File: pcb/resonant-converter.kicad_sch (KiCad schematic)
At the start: 103 parts, among them J1 Banana_Jack_Keystone_575-8, J2 Banana_Jack_Keystone_575-8, J3 Banana_Jack_Keystone_575-8, J4 Banana_Jack_Keystone_575-8, J6 Molex_KK_1x4_0470531000, Q1 MDU04N010VRH, Q2 MDU04N010VRH, Q3 HSU30N20, Q4 HSU30N20, T1 B66206W1110T001, U1 UCC256610DDBR, U2 TEA2096T/1J, U4 PC817X2CSP9F, U5 TL431AIDBVR

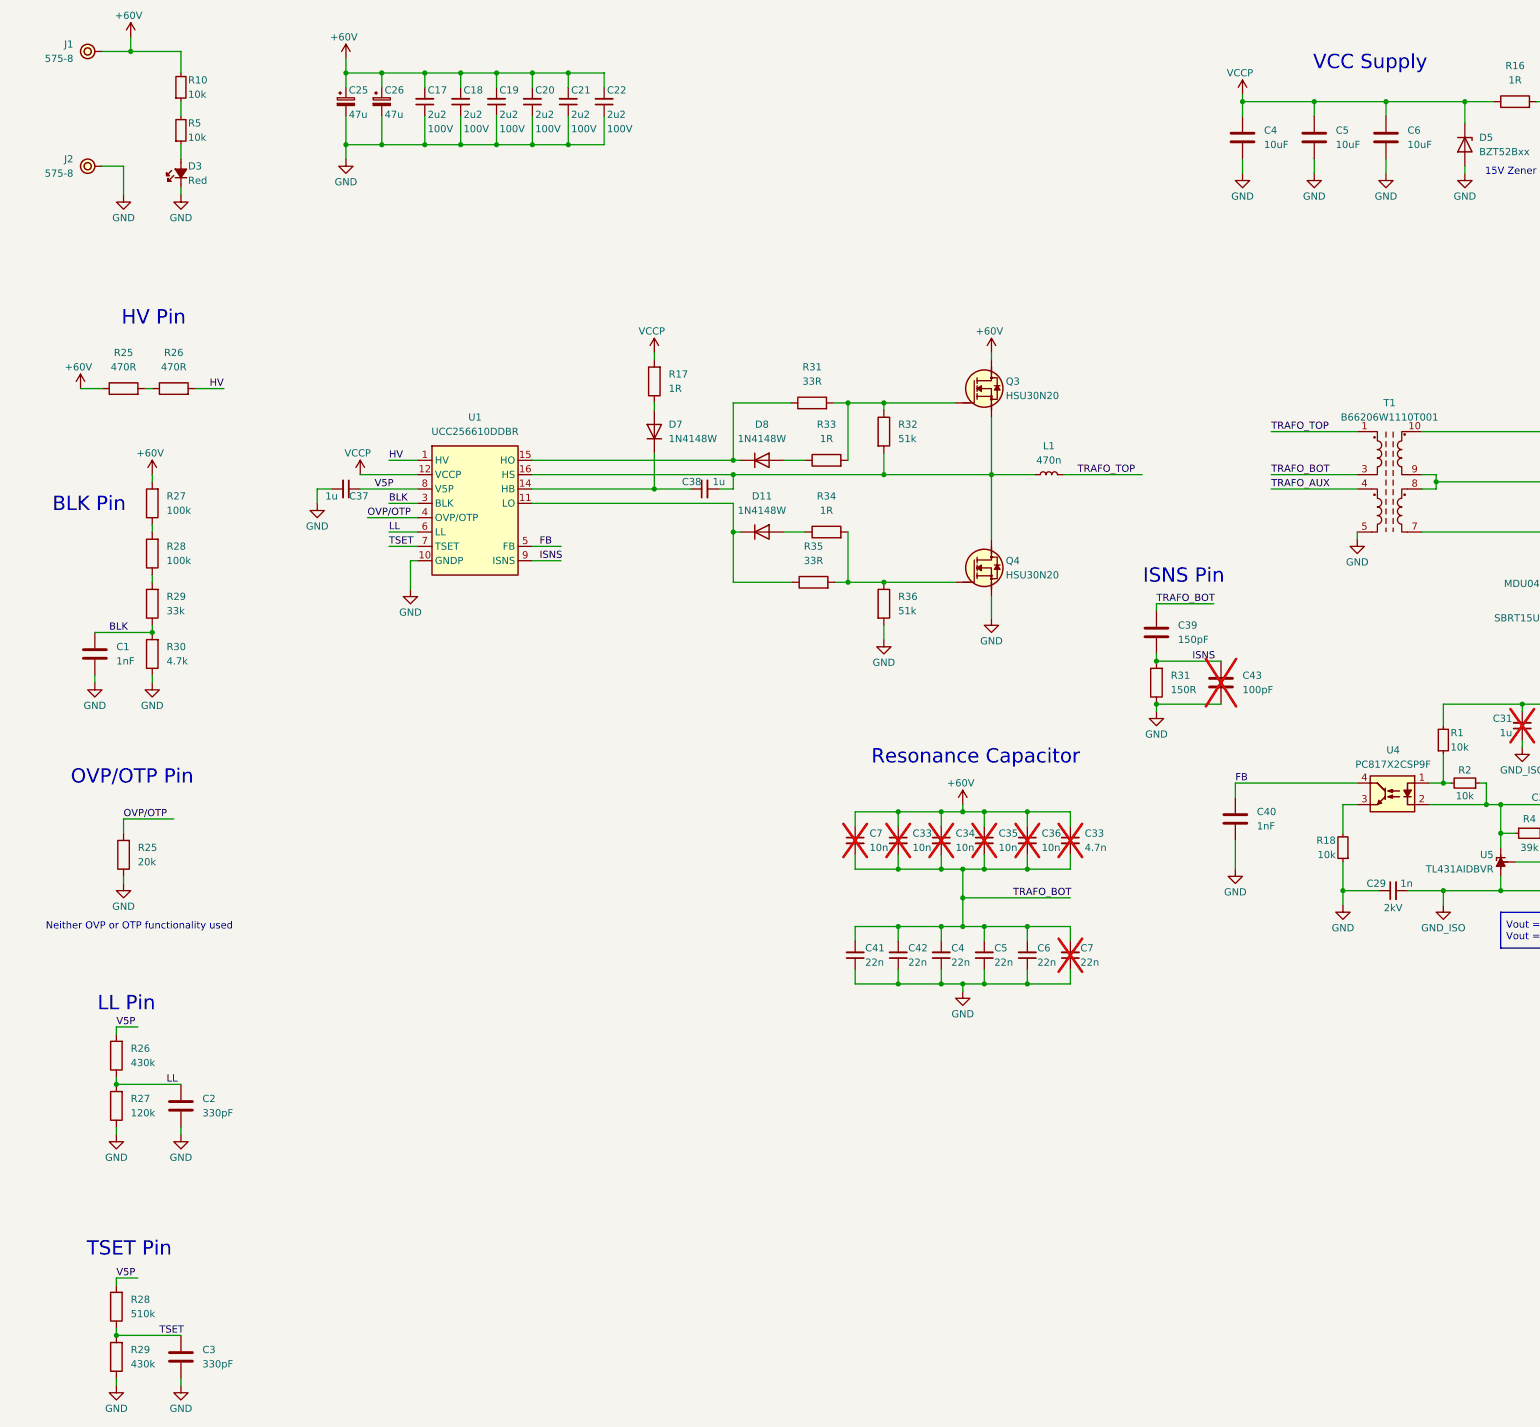
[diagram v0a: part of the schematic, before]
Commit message: Sch: Replace symbols with ones from library
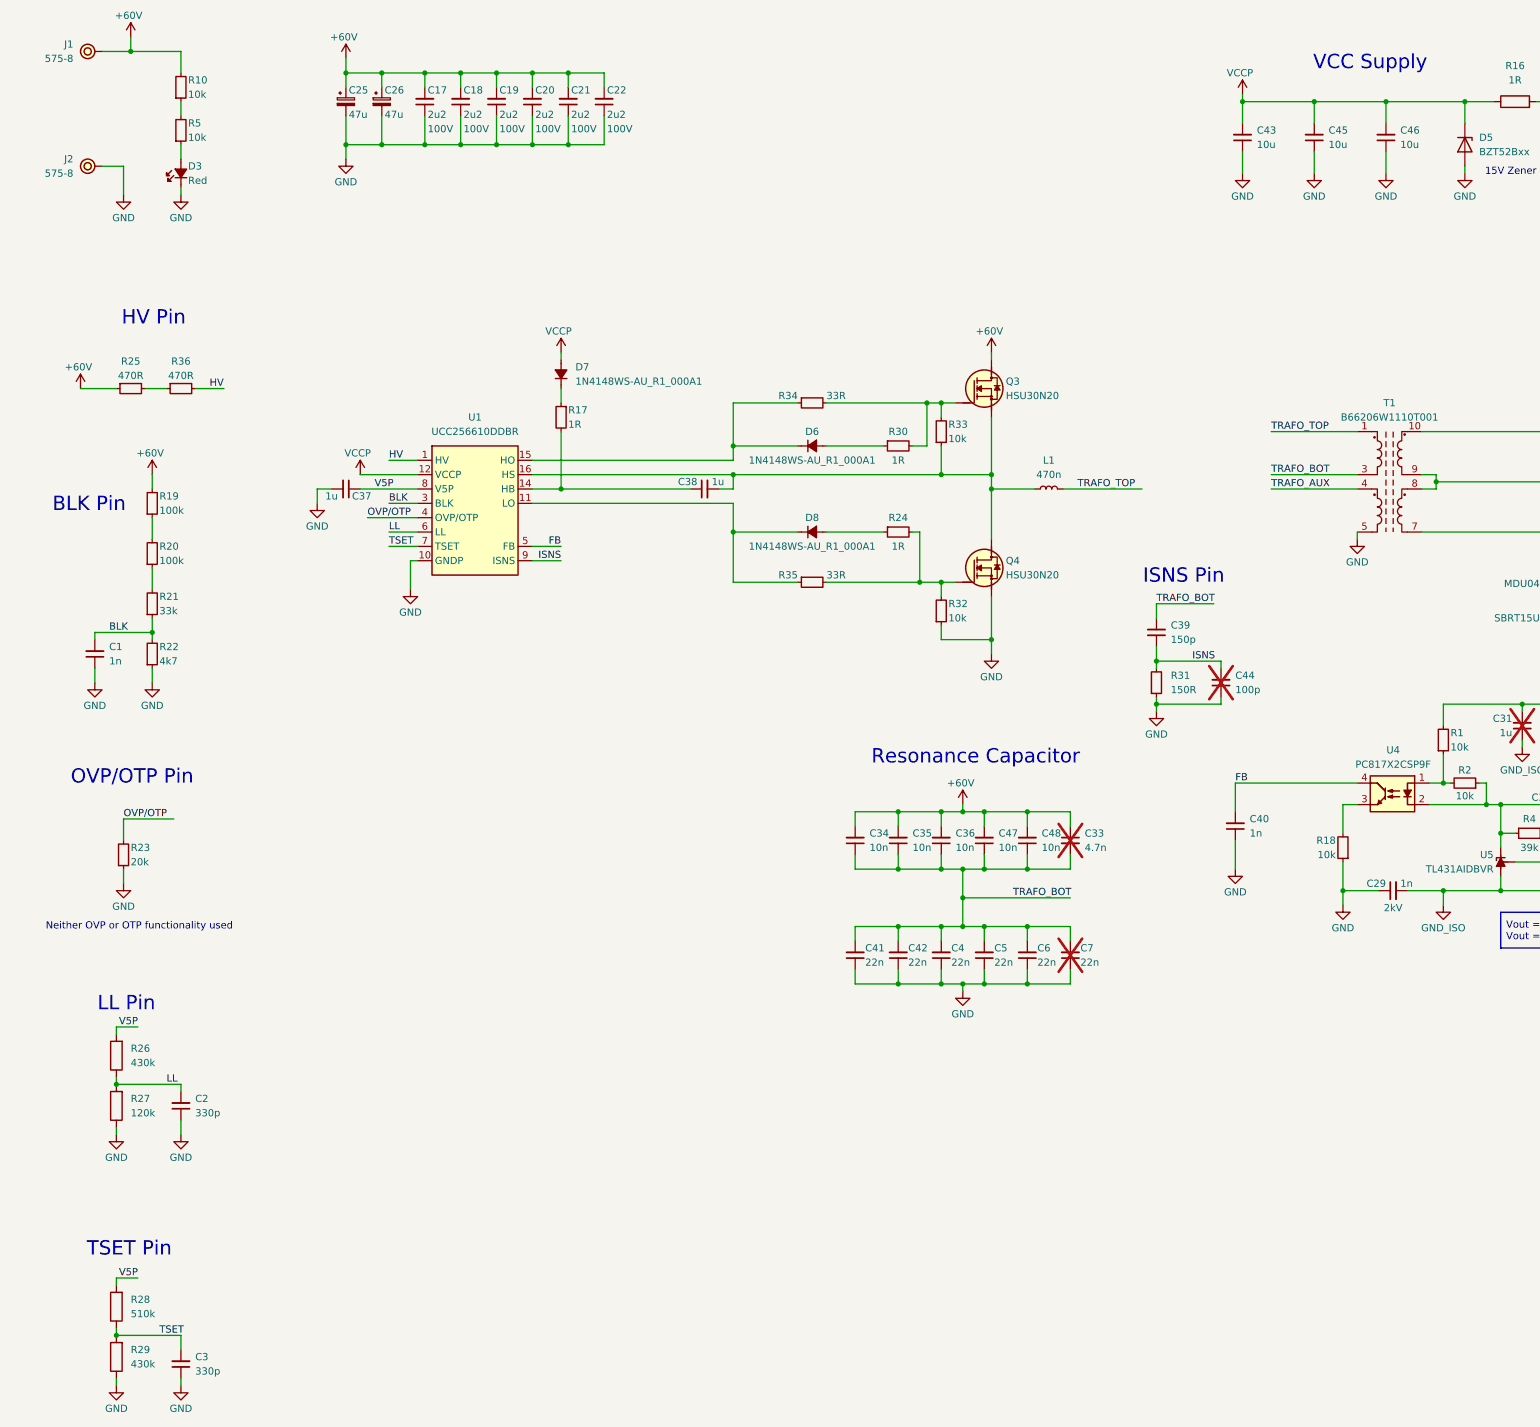
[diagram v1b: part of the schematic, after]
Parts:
- removed C1, C40: 1nF, Capacitor_SMD:C_0402_1005Metric, symbol Device:C
- removed C2, C3: 330pF, symbol Device:C
- removed C33, C34, C35, C36, C7: 10n, Capacitor_SMD:C_1206_3216Metric, symbol Device:C_Small
- removed C39: 150pF, Capacitor_SMD:C_1206_3216Metric, symbol Device:C
- removed C4, C5, C6: 10uF, Capacitor_SMD:C_0805_2012Metric, symbol Device:C
- removed C43: 100pF, Capacitor_SMD:C_0402_1005Metric, symbol Device:C
- removed D11, D7, D8: 1N4148W, Diode_SMD:D_SOD-123, symbol Diode:1N4148W
- removed R17, R33, R34: 1R, Resistor_SMD:R_0402_1005Metric, symbol Device:R
- removed R25: 20k, Resistor_SMD:R_0402_1005Metric, symbol Device:R
- removed R25, R26: 470R, Resistor_SMD:R_0402_1005Metric, symbol Device:R
- removed R27, R28: 100k, Resistor_SMD:R_0402_1005Metric, symbol Device:R
- removed R29: 33k, Resistor_SMD:R_0402_1005Metric, symbol Device:R
- removed R30: 4.7k, Resistor_SMD:R_0402_1005Metric, symbol Device:R
- removed R31: 150R, Resistor_SMD:R_0402_1005Metric, symbol Device:R
- removed R31, R35: 33R, Resistor_SMD:R_0402_1005Metric, symbol Device:R
- removed R32, R36: 51k, Resistor_SMD:R_0402_1005Metric, symbol Device:R
- added C1, C40: C-1n-0402, DW-footprints:C_0402_1005Metric, symbol DW-capacitors:C-1n-0402
- added C2, C3: C-330p-0402, DW-footprints:C_0402_1005Metric, symbol DW-capacitors:C-330p-0402
- added C34, C35, C36, C47, C48: C-10n-100V-C0G-1206, DW-footprints:C_1206_3216Metric, symbol DW-capacitors:C-10n-100V-C0G-1206
- added C39: C-150p-0402, DW-footprints:C_0402_1005Metric, symbol DW-capacitors:C-150p-0402
- added C43, C45, C46: C-10u-0805, DW-footprints:C_0805_2012Metric, symbol DW-capacitors:C-10u-0805
- added C44: C-100p-0402, DW-footprints:C_0402_1005Metric, symbol DW-capacitors:C-100p-0402
- added D6, D7, D8: 1N4148WS-AU, DW-footprints:D_SOD-323F, symbol DW-diodes:1N4148WS-AU
- added R17, R24, R30: R-1R-0603, DW-footprints:R_0603_1608Metric, symbol DW-resistors:R-1R-0603
- added R19, R20: R-100k-0402, DW-footprints:R_0402_1005Metric, symbol DW-resistors:R-100k-0402
- added R21: R-33k-0402, DW-footprints:R_0402_1005Metric, symbol DW-resistors:R-33k-0402
- added R22: R-4k7-0402, DW-footprints:R_0402_1005Metric, symbol DW-resistors:R-4k7-0402
- added R23: R-20k-0402, DW-footprints:R_0402_1005Metric, symbol DW-resistors:R-20k-0402
- added R25, R36: R-470R-0402, DW-footprints:R_0402_1005Metric, symbol DW-resistors:R-470R-0402
- added R31: R-150R-0402, DW-footprints:R_0402_1005Metric, symbol DW-resistors:R-150R-0402
- added R32, R33: R-10k-0402, DW-footprints:R_0402_1005Metric, symbol DW-resistors:R-10k-0402
- added R34, R35: R-33R-0402, DW-footprints:R_0402_1005Metric, symbol DW-resistors:R-33R-0402
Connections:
- net +60V: now also C34.2, C35.2, C36.2, C47.2, C48.2, R19.2, R25.1
- net BLK: now also C1.2, R21.1, R22.2
- net FB: now also C40.2
- net GND: now also C1.1, C2.1, C3.1, C40.1, C43.1, C44.1, C45.1, C46.1, R22.1, R23.1, R31.1, R32.1
- net HV: now also R36.2
- net ISNS: now also C39.1, C44.2, R31.2
- net LL: now also C2.2
- net OVP/OTP: now also R23.2
- net TRAFO_BOT: now also C34.1, C35.1, C36.1, C39.2, C47.1, C48.1
- net TSET: now also C3.2
- net VCCP: now also C43.2, C45.2, C46.2, D7.2 (A)
- net at C38.1, U1.14 (HB): now also R17.2
- net at C38.2, L1.1, Q3.2 (S)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: now also R33.1
- net at U1.15 (HO): now also D6.1 (C), R34.1
- net at Q3.1 (G): now also R30.2, R33.2, R34.2
- net at U1.11 (LO): now also D8.1 (C), R35.1
- net at Q4.1 (G): now also R24.2, R32.2, R35.2
- new net: D7.1 (C), R17.1
- new net: D6.2 (A), R30.1
- new net: R20.1, R21.2
- new net: D8.2 (A), R24.1
- new net: R25.2, R36.1
- new net: R19.1, R20.2
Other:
- moved on the sheet: L1

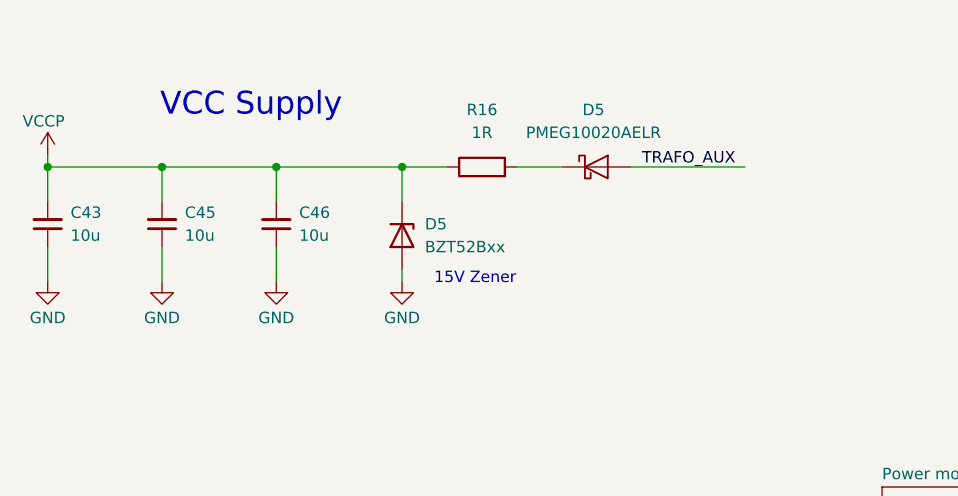
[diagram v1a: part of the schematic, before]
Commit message: Sch: Add 15V LDO for VCCP
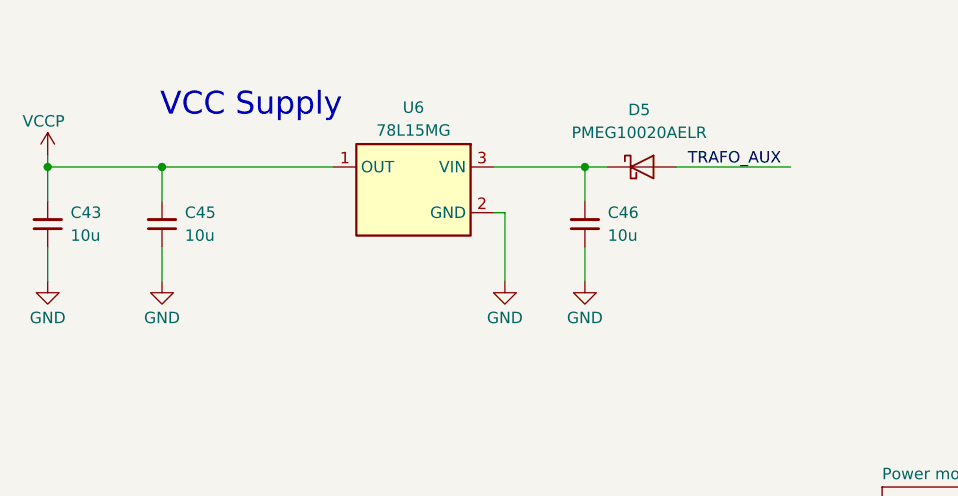
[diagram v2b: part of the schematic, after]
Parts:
- removed D5: BZT52Bxx, Diode_SMD:D_SOD-123F, symbol Diode:BZT52Bxx
- removed R16: 1R, Resistor_SMD:R_1206_3216Metric, symbol Device:R
- added U6: 78L15MG, DW-footprints:SOT-223, symbol DW-ICs:78L15MG
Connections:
- net GND: now also U6.2 (GND), U6.4 (GND)
- net VCCP: now also U6.1 (OUT); no longer C46.2
- net at D5.1 (K): now also C46.2, U6.3 (VIN)
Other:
- note removed: "15V Zener"
- moved on the sheet: C46, D5

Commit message: Update PCB from schematic, add project info block on silkscreen
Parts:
- C33: footprint Capacitor_SMD:C_1206_3216Metric -> DW-footprints:C_0402_1005Metric
- R26, R27, R28, R29: footprint Resistor_SMD:R_0402_1005Metric -> DW-footprints:R_0402_1005Metric
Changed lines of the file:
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@@
 			)
 		)
-		(property "Footprint" "Capacitor_SMD:C_1206_3216Metric"
+		(property "Footprint" "DW-footprints:C_0402_1005Metric"
 			(at 207.01 171.45 0)
 			(effects
@@
 			)
 		)
-		(property "Footprint" "Resistor_SMD:R_0402_1005Metric"
+		(property "Footprint" "DW-footprints:R_0402_1005Metric"
 			(at 39.878 209.55 90)
 			(effects
@@
 			)
 		)
-		(property "Footprint" "Resistor_SMD:R_0402_1005Metric"
+		(property "Footprint" "DW-footprints:R_0402_1005Metric"
 			(at 39.878 254 90)
 			(effects
@@
 			)
 		)
-		(property "Footprint" "Resistor_SMD:R_0402_1005Metric"
+		(property "Footprint" "DW-footprints:R_0402_1005Metric"
 			(at 39.878 218.44 90)
 			(effects
@@
 			)
 		)
-		(property "Footprint" "Resistor_SMD:R_0402_1005Metric"
+		(property "Footprint" "DW-footprints:R_0402_1005Metric"
 			(at 39.878 262.89 90)
 			(effects

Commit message: WIP: Sch: Improve readability
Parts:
- C34, C35, C36, C47, C48: now not fitted
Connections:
- net HB: now reaches C38.1, R17.2, U1.14 (HB)
- net HS: now reaches C38.2, L1.1, Q3.2 (S), Q4.3 (D), R33.1, U1.16 (HS)
- net HO: now reaches D6.1 (C), R34.1, U1.15 (HO)
- net LO: now reaches D8.1 (C), R35.1, U1.11 (LO)
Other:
- note added: "VCCP Supply"
- note removed: "HV Pin"
- note removed: "VCC Supply"
- moved on the sheet: C33, C37, C38, C39, C4, C40, C41, C42, C43, C44, C45, C46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

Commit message: Sch: Improve readability
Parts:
- removed D5: PMEG10020AELR, Diode_SMD:Nexperia_CFP3_SOD-123W, symbol Diode:PMEG10020AELR
- added D5: 1N4148WS-AU, DW-footprints:D_SOD-323F, symbol DW-diodes:1N4148WS-AU
- added D9: LED-R-0603_KT-0603R, DW-footprints:LED_0603_1608Metric_R, symbol DW-diodes:LED-R-0603_KT-0603R
- added R16: R-10k-0402, DW-footprints:R_0402_1005Metric, symbol DW-resistors:R-10k-0402
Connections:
- net GND: now also D9.1 (C)
- net TRAFO_AUX: now also D5.2 (A)
- net VCCP: now also R16.2
- net at C46.2, U6.3 (VIN): now also D5.1 (C)
- new net: D9.2 (A), R16.1
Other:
- note added: "15V 200mA"
- note added: "Primary Side"
- note added: "Secondary Side"
- note removed: "BLK Pin"
- note removed: "ISNS Pin"
- note removed: "Resonance Capacitor"
- moved on the sheet: C1, C10, C12, C13, C14, C15, C16, C17, C18, C19, C2, C20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

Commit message: Sch: Change output capacitors from 0603 to 0805
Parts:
- removed C12, C13, C14, C15, C16, C9: C-10u-0603, DW-footprints:C_0603_1608Metric, symbol DW-capacitors:C-10u-0603
- added C12, C13, C14, C15, C16, C9: C-10u-0805, DW-footprints:C_0805_2012Metric, symbol DW-capacitors:C-10u-0805
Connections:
- net +12V: now also C12.2, C13.2, C14.2, C15.2, C16.2, C9.2
- net GND_ISO: now also C12.1, C13.1, C14.1, C15.1, C16.1, C9.1

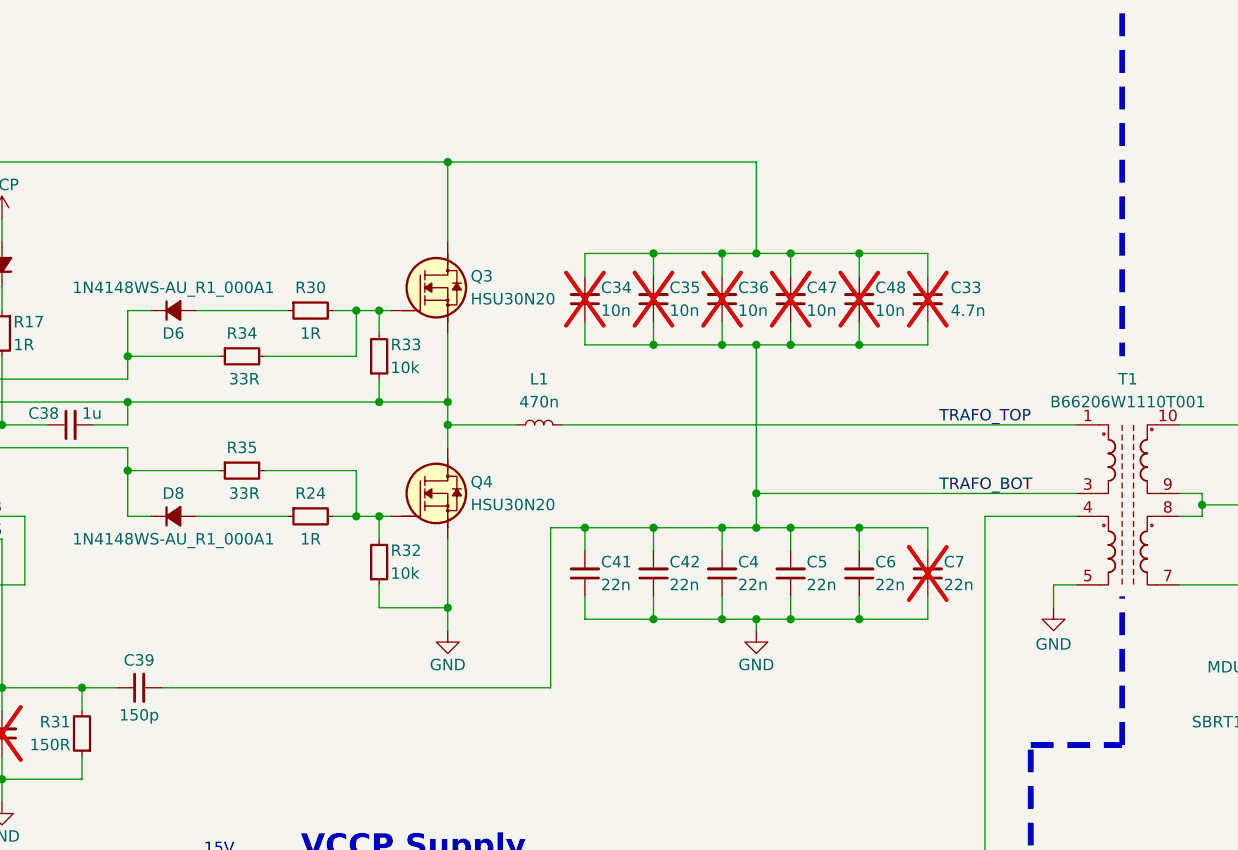
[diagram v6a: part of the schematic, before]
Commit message: Sch: Decrease spacing between resonant capacitors
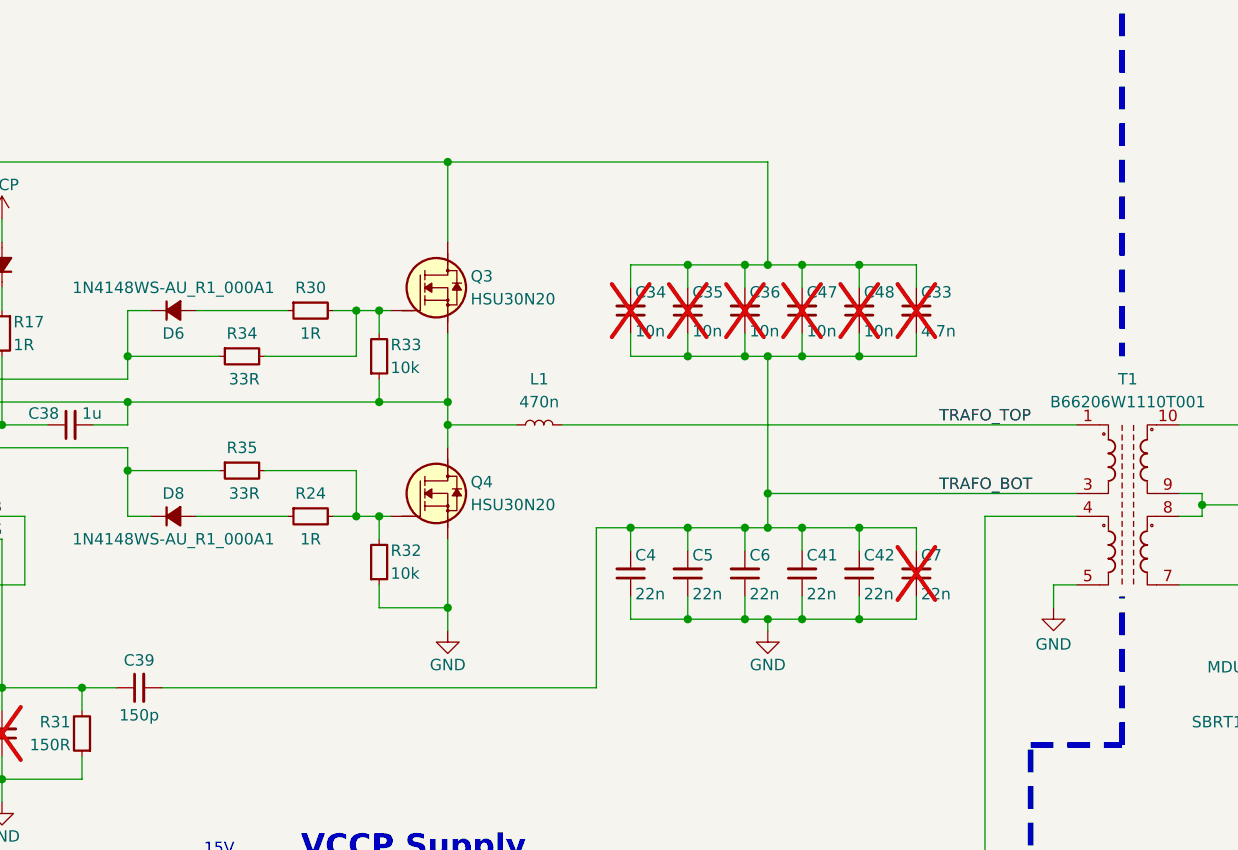
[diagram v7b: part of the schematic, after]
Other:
- moved on the sheet: C33, C34

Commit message: Re-annotate schematic, update PCB from schematic
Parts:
- renumbered C33 to C1, C18 to C10, C19 to C11, C20 to C12, C21 to C13, C22 to C14, C38 to C15, C37 to C16, C1 to C17, C4 to C18, C5 to C19, C34 to C2, C6 to C20, C41 to C21, C42 to C22, C7 to C23, C39 to C24, C44 to C25, C46 to C26, C43 to C27, C45 to C28, C2 to C29, C35 to C3, C3 to C30, C23 to C33, C24 to C34, C27 to C35, C28 to C36, C30 to C37, C9 to C38, C12 to C39, C36 to C4, C13 to C40, C14 to C41, C15 to C42, C16 to C43, C10 to C44, C40 to C45, C29 to C46, C47 to C5, C48 to C6, C25 to C7, C26 to C8, C17 to C9, D7 to D1, D6 to D2, D8 to D4, D1 to D5, D2 to D6, D5 to D7, D9 to D8, D4 to D9, J3 to J2, J2 to J3, J6 to J5, Q3 to Q1, Q4 to Q2, Q1 to Q3, Q2 to Q4, R25 to R1, R5 to R10, R21 to R11, R35 to R12, R7 to R13, R24 to R14, R22 to R15, R32 to R16, R31 to R17, R26 to R18, R28 to R19, R19 to R2, R16 to R20, R23 to R21, R27 to R22, R29 to R23, R12 to R24, R1 to R25, R3 to R26, R13 to R27, R2 to R28, R11 to R29, R36 to R3, R4 to R30, R18 to R31, R6 to R32, R17 to R4, R30 to R5, R10 to R6, R20 to R7, R34 to R8, R33 to R9, U6 to U3
